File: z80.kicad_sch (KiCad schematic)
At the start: 45 parts, among them IC4 Z80CPU, IC5 LC3664, IC901 TL974

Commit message: Some power routing.
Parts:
- added C903: 22nF, Capacitor_SMD:C_0805_2012Metric, symbol Device:C
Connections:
- net GND: now also C903.1
- net VCC1: now also C903.2
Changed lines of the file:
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@@
   (junction (at 191.77 129.54) (diameter 0) (color 0 0 0 0)
+  )
+  (junction (at 158.75 27.305) (diameter 0) (color 0 0 0 0)
   )
   (junction (at 110.49 129.54) (diameter 0) (color 0 0 0 0)
@@
     (stroke (width 0) (type default))
   )
-  (wire (pts (xy 158.75 40.64) (xy 158.75 45.085))
+  (wire (pts (xy 158.75 24.13) (xy 158.75 27.305))
     (stroke (width 0) (type default))
   )
@@
     (stroke (width 0) (type default))
   )
+  (wire (pts (xy 158.75 27.305) (xy 158.75 45.085))
+    (stroke (width 0) (type default))
+  )
   (wire (pts (xy 177.8 215.265) (xy 177.8 196.85))
     (stroke (width 0) (type default))
@@
     (stroke (width 0) (type default))
   )
+  (wire (pts (xy 167.64 27.305) (xy 158.75 27.305))
+    (stroke (width 0) (type default))
+  )
   (wire (pts (xy 222.25 114.3) (xy 222.25 127))
     (stroke (width 0) (type default))
@@
     (stroke (width 0) (type default))
   )
+  (wire (pts (xy 167.64 37.465) (xy 167.64 40.767))
+    (stroke (width 0) (type default))
+  )
   (bus (pts (xy 110.49 100.965) (xy 110.49 103.505))
     (stroke (width 0) (type default))
@@
   )
   (wire (pts (xy 125.73 212.09) (xy 118.745 212.09))
+    (stroke (width 0) (type default))
+  )
+  (wire (pts (xy 167.64 29.845) (xy 167.64 27.305))
     (stroke (width 0) (type default))
   )
@@
     (effects (font (size 2.54 2.54)) (justify left bottom))
   )
-  (label "ZD6" (at 224.79 117.475 270) (fields_autoplaced)
+  (label "ZD6" (at 224.79 118.11 270) (fields_autoplaced)
     (effects (font (size 1.27 1.27)) (justify right bottom))
   )
@@
     (effects (font (size 1.27 1.27)) (justify left bottom))
   )
-  (label "ZD7" (at 212.09 117.475 270) (fields_autoplaced)
+  (label "ZD7" (at 212.09 118.11 270) (fields_autoplaced)
     (effects (font (size 1.27 1.27)) (justify right bottom))
   )
-  (label "ZD4" (at 217.17 117.475 270) (fields_autoplaced)
+  (label "ZD4" (at 217.17 118.11 270) (fields_autoplaced)
     (effects (font (size 1.27 1.27)) (justify right bottom))
   )
@@
     (effects (font (size 1.27 1.27)) (justify left bottom))
   )
-  (label "ZD3" (at 227.33 117.475 270) (fields_autoplaced)
+  (label "ZD3" (at 227.33 118.11 270) (fields_autoplaced)
     (effects (font (size 1.27 1.27)) (justify right bottom))
   )
@@
     (effects (font (size 1.27 1.27)) (justify left bottom))
   )
-  (label "ZD1" (at 219.71 117.475 270) (fields_autoplaced)
+  (label "ZD1" (at 219.71 118.11 270) (fields_autoplaced)
     (effects (font (size 1.27 1.27)) (justify right bottom))
   )
@@
     (effects (font (size 1.27 1.27)) (justify left bottom))
   )
-  (label "ZD0" (at 209.55 117.475 270) (fields_autoplaced)
+  (label "ZD0" (at 209.55 118.11 270) (fields_autoplaced)
     (effects (font (size 1.27 1.27)) (justify right bottom))
   )
@@
     (effects (font (size 1.27 1.27)) (justify left bottom))
   )
-  (label "ZD5" (at 214.63 117.475 270) (fields_autoplaced)
+  (label "ZD5" (at 214.63 118.11 270) (fields_autoplaced)
     (effects (font (size 1.27 1.27)) (justify right bottom))
   )
-  (label "ZD2" (at 222.25 117.475 270) (fields_autoplaced)
+  (label "ZD2" (at 222.25 118.11 270) (fields_autoplaced)
     (effects (font (size 1.27 1.27)) (justify right bottom))
   )
@@
     )
   )
-  (symbol (lib_id "MegaDrive:VCC1") (at 158.75 40.64 0) (unit 1)
+  (symbol (lib_id "MegaDrive:VCC1") (at 158.75 24.13 0) (unit 1)
     (in_bom yes) (on_board yes) (dnp no) (fields_autoplaced)
-    (property "Reference" "#PWR01" (at 158.75 44.45 0)
-      (effects (font (size 1.27 1.27)) hide)
-    )
-    (property "Value" "VCC1" (at 158.75 35.56 0)
-      (effects (font (size 1.27 1.27)))
-    )
-    (property "Footprint" "" (at 158.75 40.64 0)
-      (effects (font (size 1.27 1.27)) hide)
-    )
-    (property "Datasheet" "" (at 158.75 40.64 0)
+    (property "Reference" "#PWR01" (at 158.75 27.94 0)
+      (effects (font (size 1.27 1.27)) hide)
+    )
+    (property "Value" "VCC1" (at 158.75 19.05 0)
+      (effects (font (size 1.27 1.27)))
+    )
+    (property "Footprint" "" (at 158.75 24.13 0)
+      (effects (font (size 1.27 1.27)) hide)
+    )
+    (property "Datasheet" "" (at 158.75 24.13 0)
       (effects (font (size 1.27 1.27)) hide)
     )
@@
     )
   )
+  (symbol (lib_id "power:GND") (at 167.64 40.767 0) (unit 1)
+    (in_bom yes) (on_board yes) (dnp no) (fields_autoplaced)
+    (property "Reference" "#PWR010" (at 167.64 47.117 0)
+      (effects (font (size 1.27 1.27)) hide)
+    )
+    (property "Value" "GND" (at 167.64 45.847 0)
+      (effects (font (size 1.27 1.27)))
+    )
+    (property "Footprint" "" (at 167.64 40.767 0)
+      (effects (font (size 1.27 1.27)) hide)
+    )
+    (property "Datasheet" "" (at 167.64 40.767 0)
+      (effects (font (size 1.27 1.27)) hide)
+    )
+    (pin "1")
+    (instances
+      (project "PAC_SMAIN_RE"
+        (path "/0bedf059-ca5b-49fc-a202-5049da6fe5ec"
+          (reference "#PWR010") (unit 1)
+        )
+        (path "/0bedf059-ca5b-49fc-a202-5049da6fe5ec/e6e0d8a5-d653-452c-97ca-1b76da83b141"
+          (reference "#PWR09") (unit 1)
+        )
+      )
+      (project "Neptune"
+        (path "/bcc23b51-b742-4ae5-9dd6-d96a24058944/293c8f1f-2c58-4557-aeb8-8502bb66fbd4"
+          (reference "#PWR0109") (unit 1)
+        )
+      )
+    )
+  )
   (symbol (lib_id "MegaDrive:VCC1") (at 123.19 91.44 0) (unit 1)
     (in_bom yes) (on_board yes) (dnp no) (fields_autoplaced)
@@
         )
       )
+    )
+  )
+  (symbol (lib_id "Device:C") (at 167.64 33.655 0) (mirror x) (unit 1)
+    (in_bom yes) (on_board yes) (dnp no)
+    (property "Reference" "C903" (at 171.45 33.655 90)
+      (effects (font (size 1.27 1.27)))
+    )
+    (property "Value" "22nF" (at 173.99 33.655 90)
+      (effects (font (size 1.27 1.27)))
+    )
+    (property "Footprint" "Capacitor_SMD:C_0805_2012Metric" (at 168.6052 29.845 0)
+      (effects (font (size 1.27 1.27)) hide)
+    )
+    (property "Datasheet" "~" (at 167.64 33.655 0)
+      (effects (font (size 1.27 1.27)) hide)
+    )
+    (pin "1")
+    (pin "2")
+    (instances
+      (project "Neptune"
+        (path "/bcc23b51-b742-4ae5-9dd6-d96a24058944/01513199-62c5-4123-a151-ccd381a5e6c1"
+          (reference "C903") (unit 1)
+        )
+        (path "/bcc23b51-b742-4ae5-9dd6-d96a24058944/293c8f1f-2c58-4557-aeb8-8502bb66fbd4"
+          (reference "C40") (unit 1)
+        )
+      )

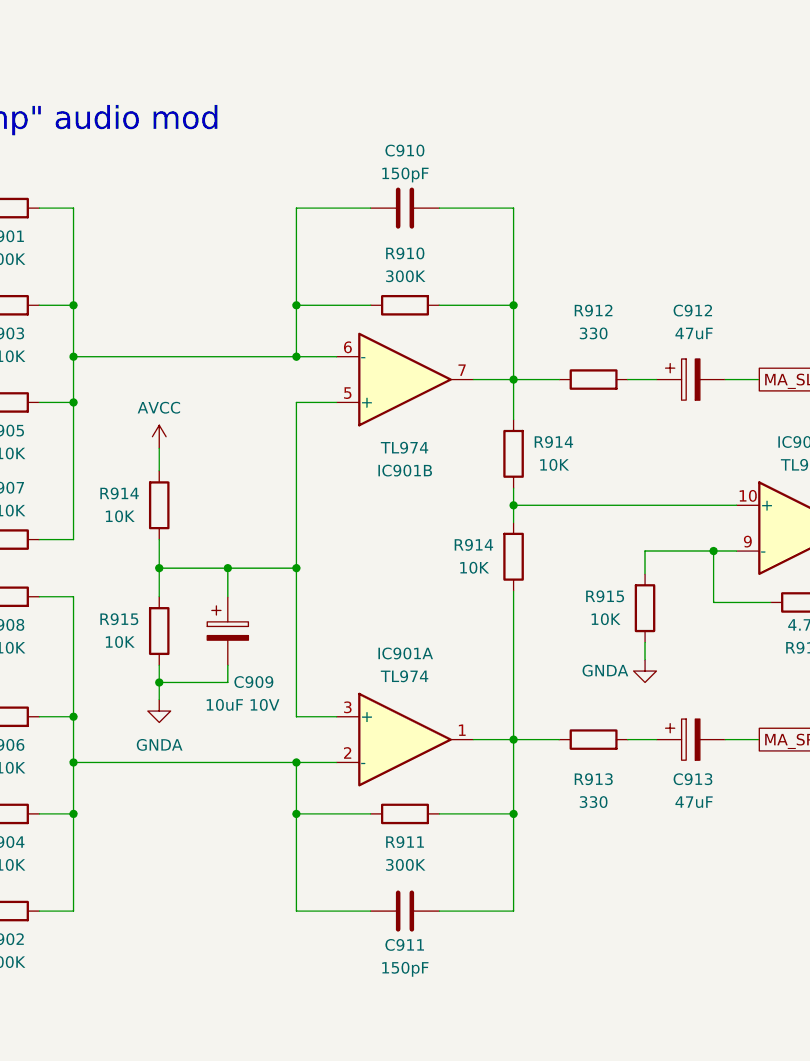
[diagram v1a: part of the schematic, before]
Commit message: BOM/footprint tweaks/corrections.
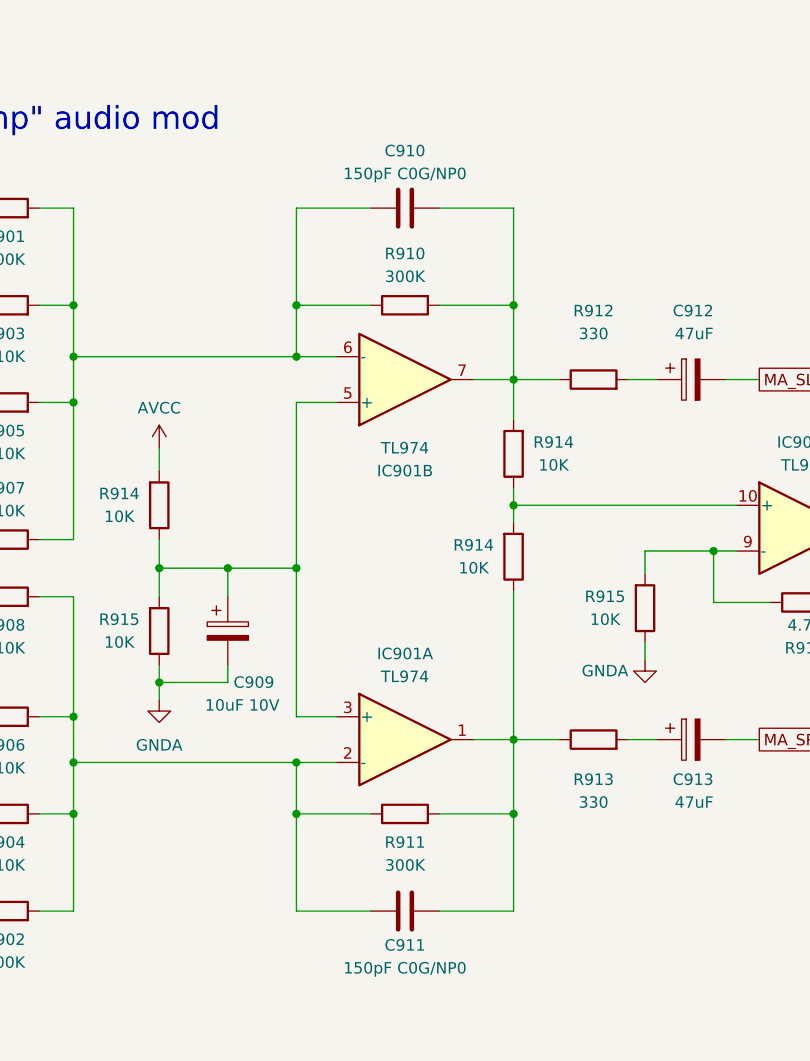
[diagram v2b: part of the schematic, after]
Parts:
- C910, C911: value 150pF -> 150pF C0G/NP0
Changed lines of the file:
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@@
       (effects (font (size 1.27 1.27)))
     )
-    (property "Value" "150pF" (at 189.865 171.45 90)
+    (property "Value" "150pF C0G/NP0" (at 189.865 171.45 90)
       (effects (font (size 1.27 1.27)))
     )
@@
       (effects (font (size 1.27 1.27)))
     )
-    (property "Value" "150pF" (at 189.865 259.715 90)
-      (effects (font (size 1.27 1.27)))
-    )
+    (property "Value" "150pF C0G/NP0" (at 189.865 259.715 90)
+      (effects (font (size 1.27 1.27)))
+    )

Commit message: General tweaks, add some DigiKey part numbers.
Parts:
- C901, C902: DigiKey (none) -> 1276-1096-1-ND
- C909: DigiKey (none) -> P15787CT-ND
- C910, C911: DigiKey (none) -> 311-4166-1-ND
- C912, C913: DigiKey (none) -> 493-13447-1-ND
- IC901: DigiKey (none) -> 296-21693-1-ND
- R903, R904, R905, R906, R907, R908: DigiKey (none) -> P210KCCT-ND
- R909, R910: DigiKey (none) -> P75.0CCT-ND
- R910, R911: DigiKey (none) -> P300KCCT-ND
- R911: DigiKey (none) -> P2.20KCCT-ND
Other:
- note added: "Integrated "Mega Amp" audio mod (with additional mono stage)"
- note removed: "Integrated "Mega Amp" audio mod"

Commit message: Enlarge some footprints, fix unwanted A/D ground connections.
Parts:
- IC4: footprint Package_QFP:LQFP-44_10x10mm_P0.8mm -> Neptune:QFP-44_10x10_Pitch0.8mm
- IC5: footprint Package_SO:SOIC-28W_7.5x18.7mm_P1.27mm -> Neptune:SOIC-28W_7.5x18.7mm_P1.27mm
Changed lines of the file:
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@@
       (effects (font (size 1.27 1.27)) (justify left))
     )
-    (property "Footprint" "Package_QFP:LQFP-44_10x10mm_P0.8mm" (at 128.27 73.025 0)
+    (property "Footprint" "Neptune:QFP-44_10x10_Pitch0.8mm" (at 128.27 73.025 0)
       (effects (font (size 1.27 1.27)) hide)
     )
@@
       (effects (font (size 1.27 1.27)) (justify left))
     )
-    (property "Footprint" "Package_SO:SOIC-28W_7.5x18.7mm_P1.27mm" (at 146.05 51.435 0)
-      (effects (font (size 1.27 1.27)) hide)
-    )
+    (property "Footprint" "Neptune:SOIC-28W_7.5x18.7mm_P1.27mm" (at 146.05 51.435 0)
+      (effects (font (size 1.27 1.27)) hide)
+    )

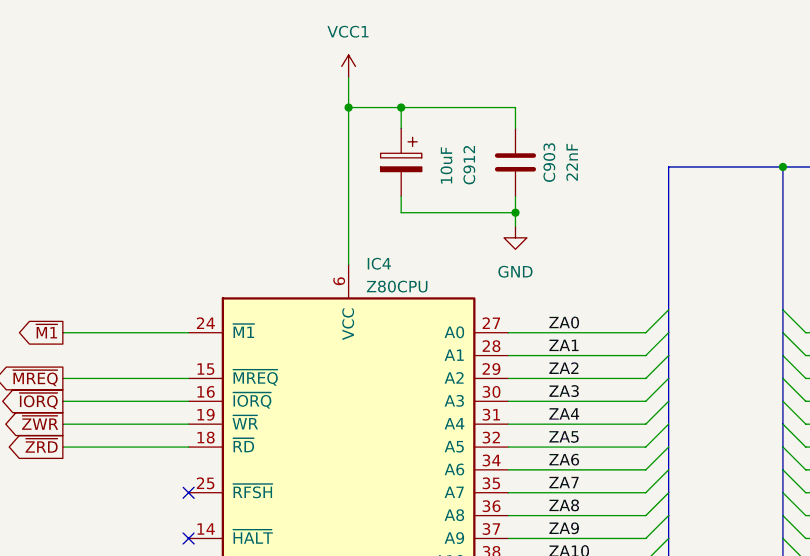
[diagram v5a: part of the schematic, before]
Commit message: Remove DRC warnings, update gerbers.
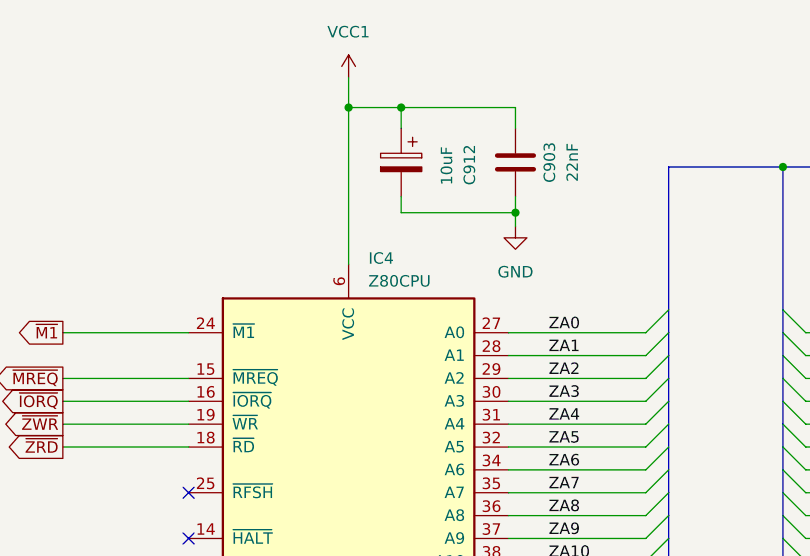
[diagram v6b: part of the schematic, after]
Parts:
- IC4: symbol MyLibrary:Z80CPU -> MegaDrive:Z80CPU
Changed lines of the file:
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@@
     )
   )
-  (symbol (lib_id "MyLibrary:Z80CPU") (at 74.93 83.185 0) (unit 1)
+  (symbol (lib_id "MegaDrive:Z80CPU") (at 74.93 83.185 0) (unit 1)
     (in_bom yes) (on_board yes) (dnp no) (fields_autoplaced)
-    (property "Reference" "IC4" (at 76.8859 45.085 0)
+    (property "Reference" "IC4" (at 77.1241 44.45 0)
       (effects (font (size 1.27 1.27)) (justify left))
     )
-    (property "Value" "Z80CPU" (at 76.8859 47.625 0)
+    (property "Value" "Z80CPU" (at 77.1241 46.99 0)
       (effects (font (size 1.27 1.27)) (justify left))
     )
@@
     (pin "1")
     (pin "10")
+    (pin "11")
     (pin "12")
     (pin "13")
@@
     (pin "15")
     (pin "16")
+    (pin "17")
     (pin "18")
     (pin "19")
@@
     (pin "31")
     (pin "32")
+    (pin "33")
     (pin "34")
     (pin "35")
@@
     (pin "37")
     (pin "38")
+    (pin "39")
     (pin "4")
     (pin "40")

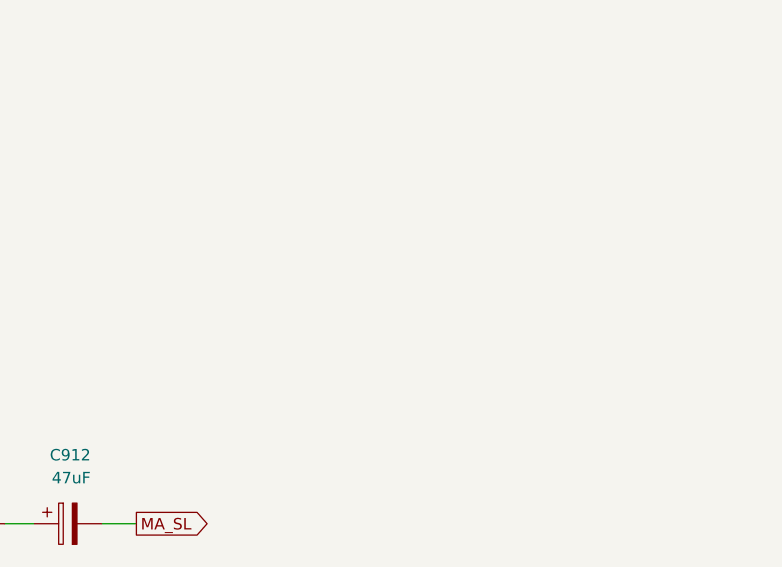
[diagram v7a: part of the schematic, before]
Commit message: Use 32X reset(s) for MD side.
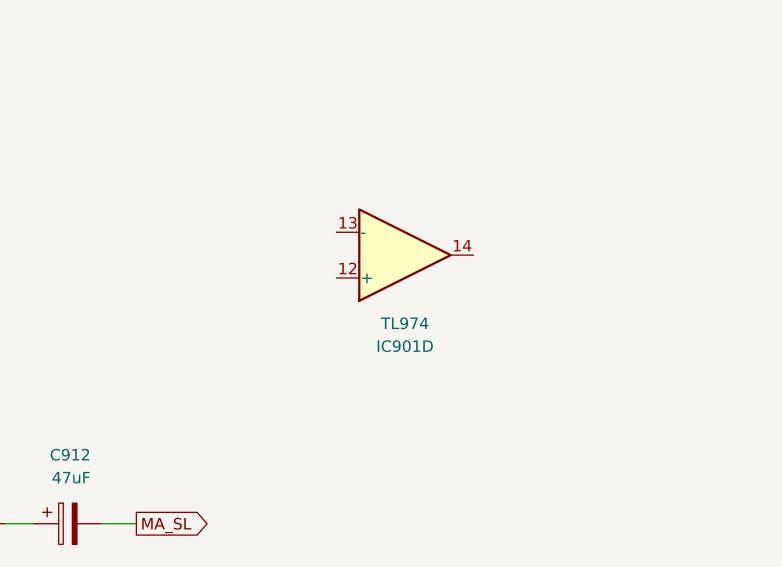
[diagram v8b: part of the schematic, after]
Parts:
- added unit 4 of IC901
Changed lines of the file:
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@@
+    )
+  )
+  (symbol (lib_id "Amplifier_Operational:TL064") (at 259.08 164.465 0) (mirror x) (unit 4)
+    (in_bom yes) (on_board yes) (dnp no)
+    (property "Reference" "IC901" (at 259.08 174.625 0)
+      (effects (font (size 1.27 1.27)))
+    )
+    (property "Value" "TL974" (at 259.08 172.085 0)
+      (effects (font (size 1.27 1.27)))
+    )
+    (property "Footprint" "Package_SO:SO-14_3.9x8.65mm_P1.27mm" (at 257.81 167.005 0)
+      (effects (font (size 1.27 1.27)) hide)
+    )
+    (property "Datasheet" "http://www.ti.com/lit/ds/symlink/tl061.pdf" (at 260.35 169.545 0)
+      (effects (font (size 1.27 1.27)) hide)
+    )
+    (property "DigiKey" "296-21693-1-ND" (at 259.08 164.465 0)
+      (effects (font (size 1.27 1.27)) hide)
+    )
+    (pin "1")
+    (pin "2")
+    (pin "3")
+    (pin "5")
+    (pin "6")
+    (pin "7")
+    (pin "10")
+    (pin "8")
+    (pin "9")
+    (pin "12")
+    (pin "13")
+    (pin "14")
+    (pin "11")
+    (pin "4")
+    (instances
+      (project "Neptune"
+        (path "/bcc23b51-b742-4ae5-9dd6-d96a24058944/293c8f1f-2c58-4557-aeb8-8502bb66fbd4"
+          (reference "IC901") (unit 4)
+        )
+      )
     )
   )
